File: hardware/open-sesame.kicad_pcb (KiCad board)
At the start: 2 copper layers, 72.2 x 45 mm, 9 parts, among them J1 Conn_01x10, J3 Barrel_Jack_Switch, J4 Conn_01x06_Socket

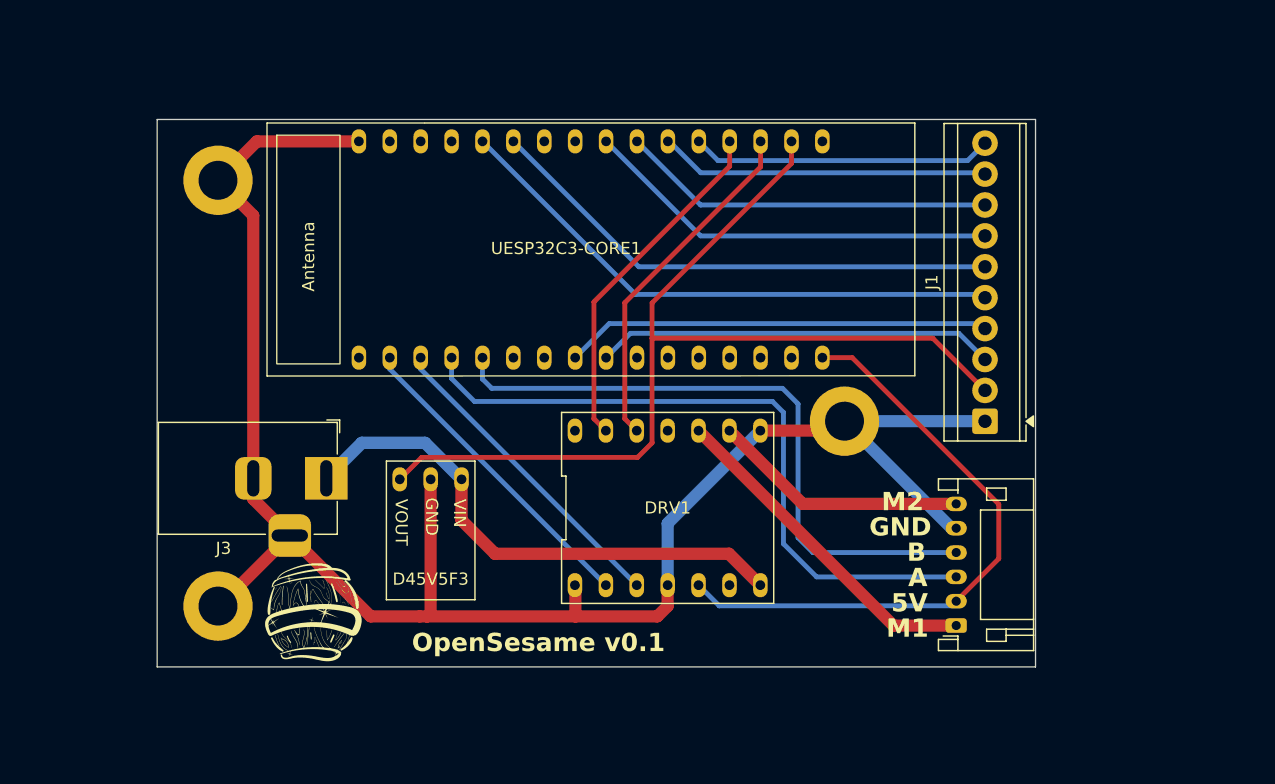
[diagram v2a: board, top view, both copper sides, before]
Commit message: User Terminals, Added Optocoupler, Added QWIIC connector
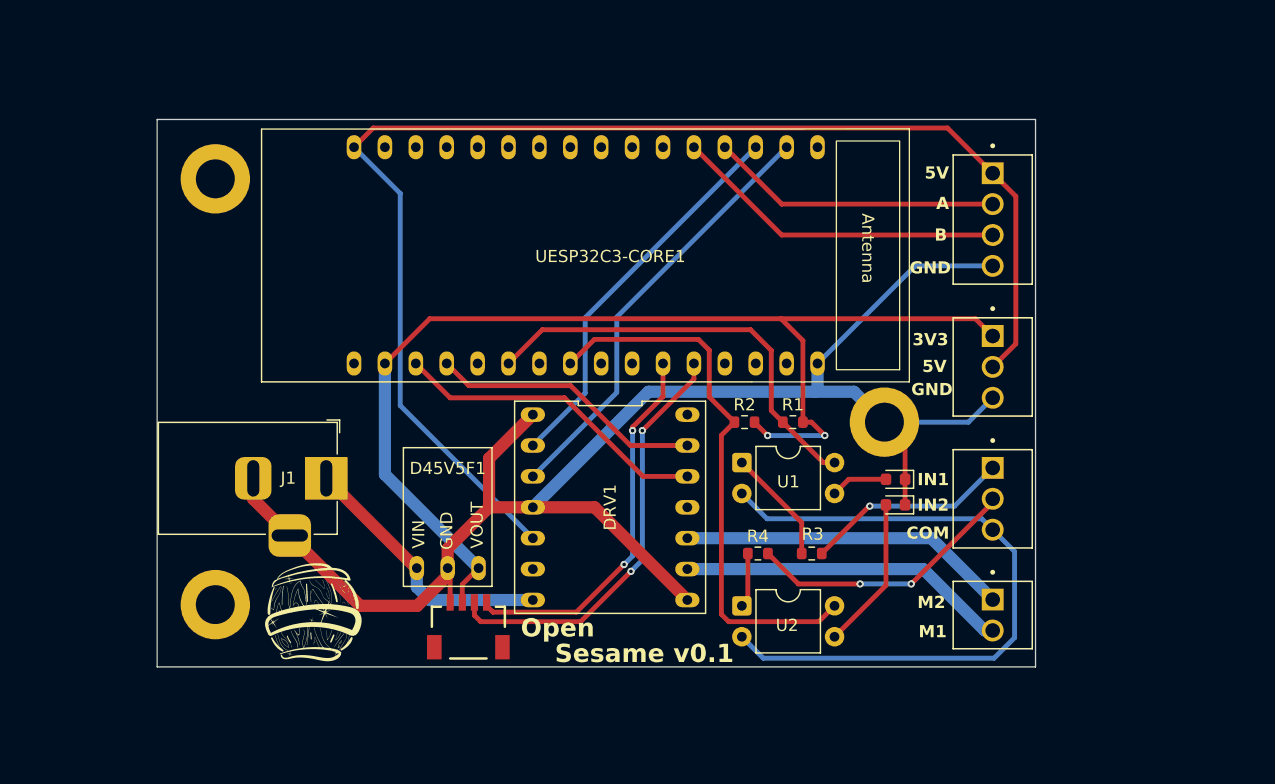
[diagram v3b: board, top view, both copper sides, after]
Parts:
- removed D45V5F3: D45V5F3, Library:D45V5Fx
- removed the J1 at (188.9, 92.4)
- added D1: LED, LED_SMD:LED_0603_1608Metric, F.Cu at (181.5, 97.2)
- added D2: LED, LED_SMD:LED_0603_1608Metric, F.Cu at (181.5, 99.3)
- added D45V5F1: D45V5F3, MyLibrary:D45V5Fx, F.Cu at (144.7, 104.5)
- added J2: Screw_Terminal_01x02, MyLibrary:TE_282834-2, F.Cu at (189.5, 108.4)
- added J3: Screw_Terminal_01x04, MyLibrary:TE_282834-4, F.Cu at (189.5, 75.8)
- added J5: Screw_Terminal_01x03, MyLibrary:TE_282834-3, F.Cu at (189.5, 88.0)
- added J6: Qwiic_RA, SparkFun-Connector:JST_1x04_P1.0mm_Horizontal_SMD, F.Cu at (146.4, 107.3)
- added R1: 10k, Resistor_SMD:R_0603_1608Metric, F.Cu at (173.1, 92.5)
- added R2: 10k, Resistor_SMD:R_0603_1608Metric, F.Cu at (169.1, 92.5)
- added R3: 4.7k, Resistor_SMD:R_0603_1608Metric, F.Cu at (174.6, 103.3)
- added R4: 4.7k, Resistor_SMD:R_0603_1608Metric, F.Cu at (170.2, 103.3)
- added U1: PC817, Package_DIP:DIP-4_W7.62mm, F.Cu at (168.9, 95.8)
- added U2: PC817, Package_DIP:DIP-4_W7.62mm, F.Cu at (168.9, 107.6)
- DRV1: footprint Library:DRV8874 -> MyLibrary:DRV8874
- J4: value Conn_01x06_Socket -> Screw_Terminal_01x03; footprint Connector_JST:JST_PH_S6B-PH-K_1x06_P2.00mm_Horizontal -> MyLibrary:TE_282834-3
- UESP32C3-CORE1: footprint Library:LUATOS_ESP32C3 -> MyLibrary:LUATOS_ESP32C3
- moved J4 10.8 mm to (189.5, 98.8), turned to -90 degrees
- moved DRV1 4.73 mm to (158.1, 99.5), turned to -90 degrees
- moved H2 3.28 mm to (180.6, 92.5)
- moved UESP32C3-CORE1 0.62 mm to (156.1, 78.8), turned to 180 degrees
- moved H1 0.25 mm to (125.6, 72.5)
- moved H3 0.25 mm to (125.6, 107.5), turned to 90 degrees
- renumbered J3 to J1
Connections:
- DRV1 pad 2: Net-(DRV1-EN/IN1) -> EN
- DRV1 pad 3: Net-(DRV1-PH/IN2) -> PH
- J4 pad 1: M2 -> IN1
- J4 pad 2: +5V -> IN2
- J4 pad 3: A -> IN_COMMON
- UESP32C3-CORE1 pad 2: Net-(DRV1-EN/IN1) -> PH
- UESP32C3-CORE1 pad 21: Net-(J1-Pin_10) -> unconnected-(UESP32C3-CORE1-GPIO10/SPI_MISO-Pad21)
- UESP32C3-CORE1 pad 22: Net-(J1-Pin_9) -> GPIO6
- UESP32C3-CORE1 pad 23: Net-(J1-Pin_8) -> unconnected-(UESP32C3-CORE1-GPIO07/SPI_CS-Pad23)
- UESP32C3-CORE1 pad 24: Net-(J1-Pin_7) -> GPIO11
- UESP32C3-CORE1 pad 27: Net-(J1-Pin_6) -> SCL
- UESP32C3-CORE1 pad 28: Net-(J1-Pin_5) -> SDA
- UESP32C3-CORE1 pad 3: Net-(DRV1-PH/IN2) -> EN
- UESP32C3-CORE1 pad 8: Net-(J1-Pin_4) -> unconnected-(UESP32C3-CORE1-UART0_RX-Pad8)
- UESP32C3-CORE1 pad 9: Net-(J1-Pin_3) -> unconnected-(UESP32C3-CORE1-UART0_TX-Pad9)
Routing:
- net +5V: track 50.4 -> 110.4 mm
- net IN_COMMON: track 0.00 -> 55.3 mm
- net Net-(J1-Pin_5): track 46.2 -> 0.00 mm
- net GPIO11: track 0.00 -> 45.7 mm
- net Net-(J1-Pin_6): track 43.0 -> 0.00 mm
- net PH: track 0.00 -> 35.7 mm
- net GPIO6: track 0.00 -> 35.4 mm
- net SDA: track 0.00 -> 35.1 mm, vias 0 -> 2
- net Net-(J1-Pin_4): track 34.4 -> 0.00 mm
- net Net-(J1-Pin_7): track 34.4 -> 0.00 mm
- net Net-(J1-Pin_3): track 32.9 -> 0.00 mm
- net A: track 56.3 -> 24.0 mm
- net EN: track 0.00 -> 32.1 mm
- net SCL: track 0.00 -> 31.3 mm, vias 0 -> 2
- net Net-(J1-Pin_8): track 30.8 -> 0.00 mm
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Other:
- board text added: "3V3"
- board text added: "COM"
- board text added: "IN1"
- board text added: "IN2"
- board text added: "Open"
- board text added: "Sesame v0.1"
- board text removed: "OpenSesame v0.1"

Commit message: Use 2x 6 port connectors
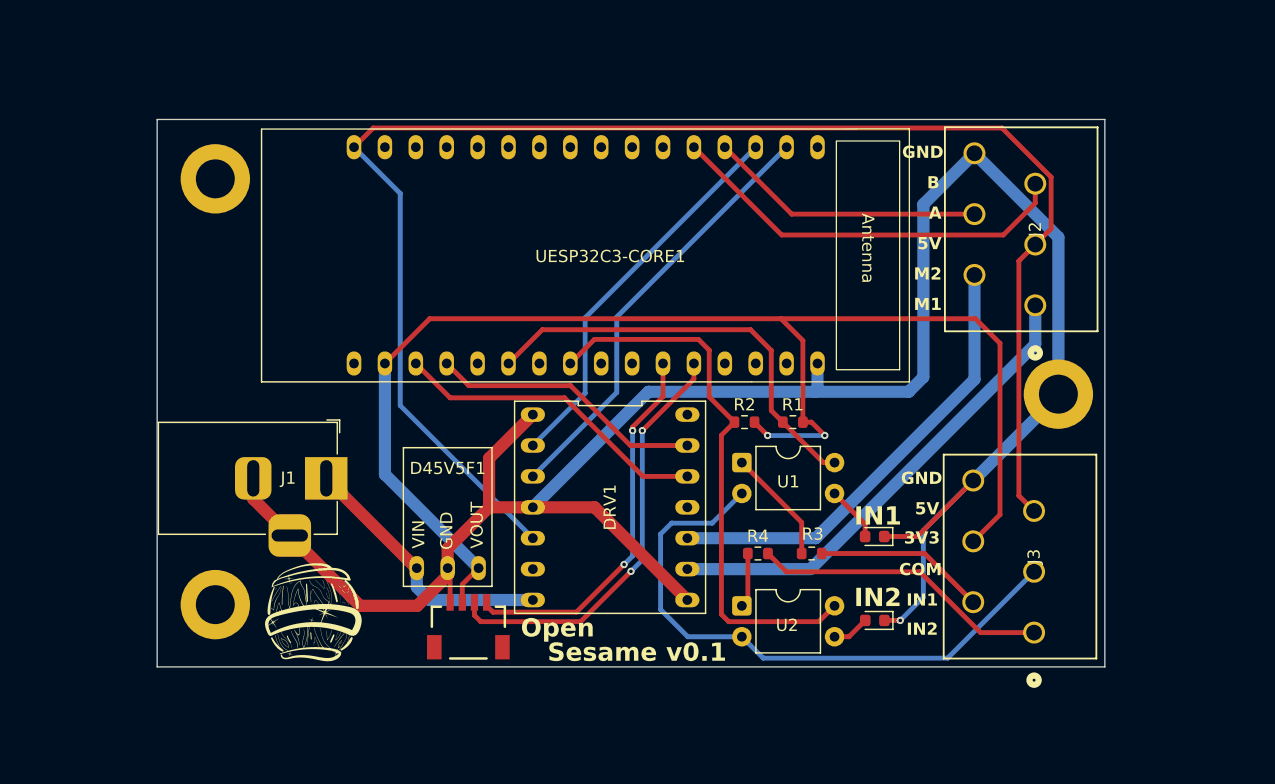
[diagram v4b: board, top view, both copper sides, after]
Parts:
- removed the J4 at (189.5, 98.8)
- removed J5: Screw_Terminal_01x03, MyLibrary:TE_282834-3
- J2: value Screw_Terminal_01x02 -> 1-2834021-6; footprint MyLibrary:TE_282834-2 -> TE-Connectivity-Connector:CONN6_1-2834021-6_TEC
- J3: value Screw_Terminal_01x04 -> 1-2834021-6; footprint MyLibrary:TE_282834-4 -> TE-Connectivity-Connector:CONN6_1-2834021-6_TEC
- moved J3 34.1 mm to (192.9, 109.8), turned to 90 degrees
- moved J2 25.7 mm to (193.0, 82.9), turned to 90 degrees
- moved H2 14.5 mm to (194.9, 90.2)
- moved D2 9.65 mm to (179.8, 108.8)
- moved D1 5.00 mm to (179.8, 101.9)
- renumbered J6 to J4
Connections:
- J2 pad 1: M2 -> M1
- J2 pad 2: M1 -> M2
- J3 pad 1: +5V -> IN2
- J3 pad 2: A -> IN1
- J3 pad 3: B -> IN_COMMON
- J3 pad 4: GND -> +3V3
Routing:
- net GND: track 129.7 -> 177.2 mm, vias 0 -> 1
- net +3V3: track 93.2 -> 111.2 mm
- net +5V: track 110.4 -> 126.9 mm
- net M1: track 27.2 -> 39.5 mm
- net M2: track 27.2 -> 37.6 mm
- net Net-(D2-A): track 12.6 -> 3.08 mm
- net B: track 27.5 -> 33.7 mm
- net IN_COMMON: track 55.3 -> 49.6 mm
- net IN1: track 17.0 -> 14.1 mm, vias 1 -> 0
- net IN2: track 22.3 -> 24.6 mm, vias 2 -> 0
- net A: track 24.0 -> 22.8 mm
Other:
- board size 72.2 x 45 mm -> 77.9 x 45 mm

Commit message: hardware: Use ESP32S3 for PCNT,
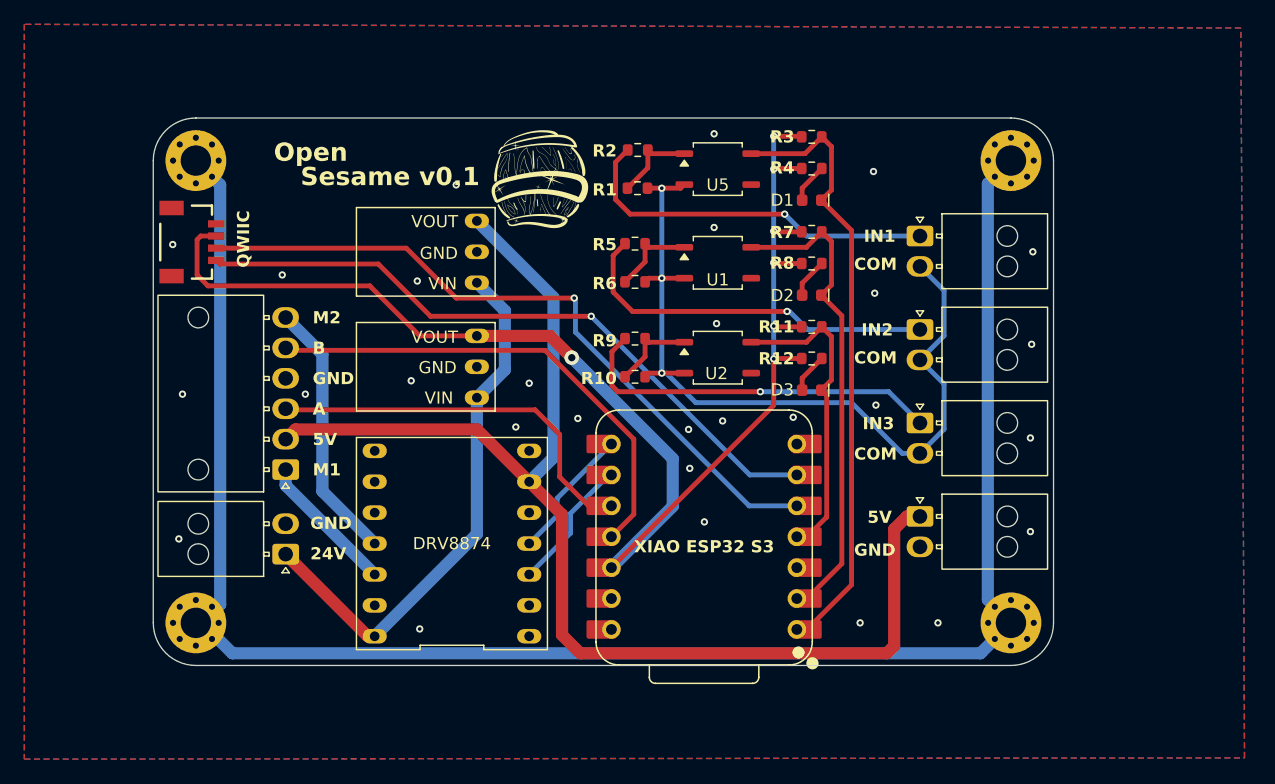
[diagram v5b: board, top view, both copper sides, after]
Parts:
- removed DRV1: DRV8874, MyLibrary:DRV8874
- removed UESP32C3-CORE1: ~, MyLibrary:LUATOS_ESP32C3
- added D3: LED, SparkFun-LED:LED_0603_1608Metric, F.Cu at (174.6, 89.9)
- added D45V5F2: D45V5F3, MyLibrary:D45V5Fx, F.Cu at (147.1, 88.0)
- added DRV8874: DRV8874, MyLibrary:DRV8874, F.Cu at (145.1, 102.5)
- added H4: MountingHole_Pad, MountingHole:MountingHole_2.5mm_Pad_Via, F.Cu at (124.0, 109.0)
- added J5: Conn_01x02, Connector_Molex:Molex_Nano-Fit_105313-xx02_1x02_P2.50mm_Horizontal, F.Cu at (183.5, 84.9)
- added J6: Conn_01x02, Connector_Molex:Molex_Nano-Fit_105313-xx02_1x02_P2.50mm_Horizontal, F.Cu at (183.5, 92.6)
- added J7: Qwiic_RA, SparkFun-Connector:JST_1x04_P1.0mm_Horizontal_SMD, F.Cu at (125.7, 77.7)
- added R10: 750R, Resistor_SMD:R_0603_1608Metric, F.Cu at (160.1, 88.8)
- added R11: 10k, Resistor_SMD:R_0603_1608Metric, F.Cu at (174.6, 84.7)
- added R12: 270R, Resistor_SMD:R_0603_1608Metric, F.Cu at (174.6, 87.3)
- added R5: 750R, Resistor_SMD:R_0603_1608Metric, F.Cu at (160.1, 77.8)
- added R6: 750R, Resistor_SMD:R_0603_1608Metric, F.Cu at (160.1, 81.0)
- added R7: 10k, Resistor_SMD:R_0603_1608Metric, F.Cu at (174.6, 76.9)
- added R8: 270R, Resistor_SMD:R_0603_1608Metric, F.Cu at (174.6, 79.5)
- added R9: 750R, Resistor_SMD:R_0603_1608Metric, F.Cu at (160.1, 85.6)
- added U5: CPC1019N, Package_SO:SOP-4_3.8x4.1mm_P2.54mm, F.Cu at (166.9, 71.7)
- added XIAO ESP32 S3: XIAO-ESP32-S3-DIP, XIAO_Series_Footprints:XIAO-ESP32-S3-DIP, F.Cu at (165.8, 101.9)
- D1, D2: footprint LED_SMD:LED_0603_1608Metric -> SparkFun-LED:LED_0603_1608Metric
- D45V5F1: value D45V5F3 -> D45V5F5
- H1, H2, H3: footprint MountingHole:MountingHole_3.2mm_M3_ISO7380_Pad -> MountingHole:MountingHole_2.5mm_Pad_Via
- J1: value Barrel_Jack_Switch -> Conn_01x02; footprint Connector_BarrelJack:BarrelJack_Horizontal -> Connector_Molex:Molex_Nano-Fit_105313-xx02_1x02_P2.50mm_Horizontal
- J2: value 1-2834021-6 -> Conn_01x06; footprint TE-Connectivity-Connector:CONN6_1-2834021-6_TEC -> Connector_Molex:Molex_Nano-Fit_105313-xx06_1x06_P2.50mm_Horizontal
- J3: value 1-2834021-6 -> Conn_01x02; footprint TE-Connectivity-Connector:CONN6_1-2834021-6_TEC -> Connector_Molex:Molex_Nano-Fit_105313-xx02_1x02_P2.50mm_Horizontal
- J4: value Qwiic_RA -> Conn_01x02; footprint SparkFun-Connector:JST_1x04_P1.0mm_Horizontal_SMD -> Connector_Molex:Molex_Nano-Fit_105313-xx02_1x02_P2.50mm_Horizontal
- R1, R2: value 10k -> 750R
- R3: value 4.7k -> 10k
- R4: value 4.7k -> 270R
- U1, U2: value PC817 -> CPC1019N; footprint Package_DIP:DIP-4_W7.62mm -> Package_SO:SOP-4_3.8x4.1mm_P2.54mm
- moved H1 65.4 mm to (191.0, 71.0)
- moved J2 63.1 mm to (131.4, 96.4), turned to 180 degrees
- moved J4 47.8 mm to (183.5, 77.2)
- moved H3 36.5 mm to (124.0, 71.0), turned to 0 degrees
- moved R3 34.2 mm to (174.6, 69.0)
- moved R4 32.0 mm to (174.6, 71.7)
- moved D1 28.1 mm to (174.6, 74.3)
- moved D2 27.2 mm to (174.6, 82.1)
- moved D45V5F1 26.1 mm to (147.1, 78.5), turned to 90 degrees
- moved R2 24.0 mm to (160.3, 70.1)
- moved R1 23.1 mm to (160.3, 73.3)
- moved U2 20.5 mm to (166.9, 87.2)
- moved H2 19.2 mm to (191.0, 109.0)
- moved U1 16.5 mm to (166.9, 79.4)
- moved J3 13.4 mm to (183.5, 100.2), turned to 0 degrees
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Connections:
- D1 pad 1: GND -> GPIO1
- D2 pad 1: GND -> GPIO2
- D45V5F1 pad 3: +3V3 -> +5V
- H1 pad 1: GND -> Earth
- H2 pad 1: GND -> Earth
- H3 pad 1: GND -> Earth
- J2 pad 2: M2 -> +5V
- J2 pad 3: +5V -> A
- J2 pad 4: A -> GND
- J2 pad 6: GND -> M2
- J3 pad 1: IN2 -> +5V
- J3 pad 2: IN1 -> GND
- J4 pad 1: GND -> IN1
- J4 pad 2: +3V3 -> IN_COMMON
- R1 pad 1: GPIO6 -> Net-(R1-Pad1)
- R1 pad 2: +3V3 -> IN_COMMON
- R2 pad 1: GPIO11 -> IN1
- R2 pad 2: +3V3 -> Net-(R1-Pad1)
- R3 pad 1: Net-(R3-Pad1) -> +3V3
- R3 pad 2: IN1 -> GPIO1
- R4 pad 1: Net-(R4-Pad1) -> +3V3
- R4 pad 2: IN2 -> Net-(D1-A)
- U1 pad 1: Net-(R3-Pad1) -> Net-(R5-Pad2)
- U1 pad 3: Net-(D1-A) -> GND
- U1 pad 4: GPIO6 -> GPIO2
- U2 pad 1: Net-(R4-Pad1) -> Net-(R10-Pad1)
- U2 pad 3: Net-(D2-A) -> GND
- U2 pad 4: GPIO11 -> GPIO4
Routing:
- net GND: track 177.2 -> 0.00 mm, vias 1 -> 29
- net Earth: track 0.00 -> 147.6 mm
- net GPIO1: track 0.00 -> 51.2 mm
- net GPIO11: track 45.7 -> 0.00 mm
- net GPIO2: track 0.00 -> 39.0 mm
- net GPIO6: track 35.4 -> 0.00 mm
- net IN3: track 0.00 -> 30.9 mm, vias 0 -> 1
- net M1: track 39.5 -> 11.7 mm
- net FAULT: track 26.2 -> 0.00 mm
- net +5V: track 126.9 -> 101.1 mm
- net GPIO4: track 0.00 -> 25.1 mm
- net PH: track 35.7 -> 11.0 mm
- net SCL: track 31.3 -> 55.0 mm, vias 2 -> 1
- net SDA: track 35.1 -> 58.1 mm, vias 2 -> 1
- net CS: track 22.6 -> 0.00 mm
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- added copper zone on B.Cu, net GND
- added copper zone on F.Cu, net GND
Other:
- board size 77.9 x 45 mm -> 74 x 45 mm
- board text added: "24V"
- board text added: "IN3"
- board text added: "QWIIC"
- board text removed: "3V3"

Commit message: hardware: shrunk board
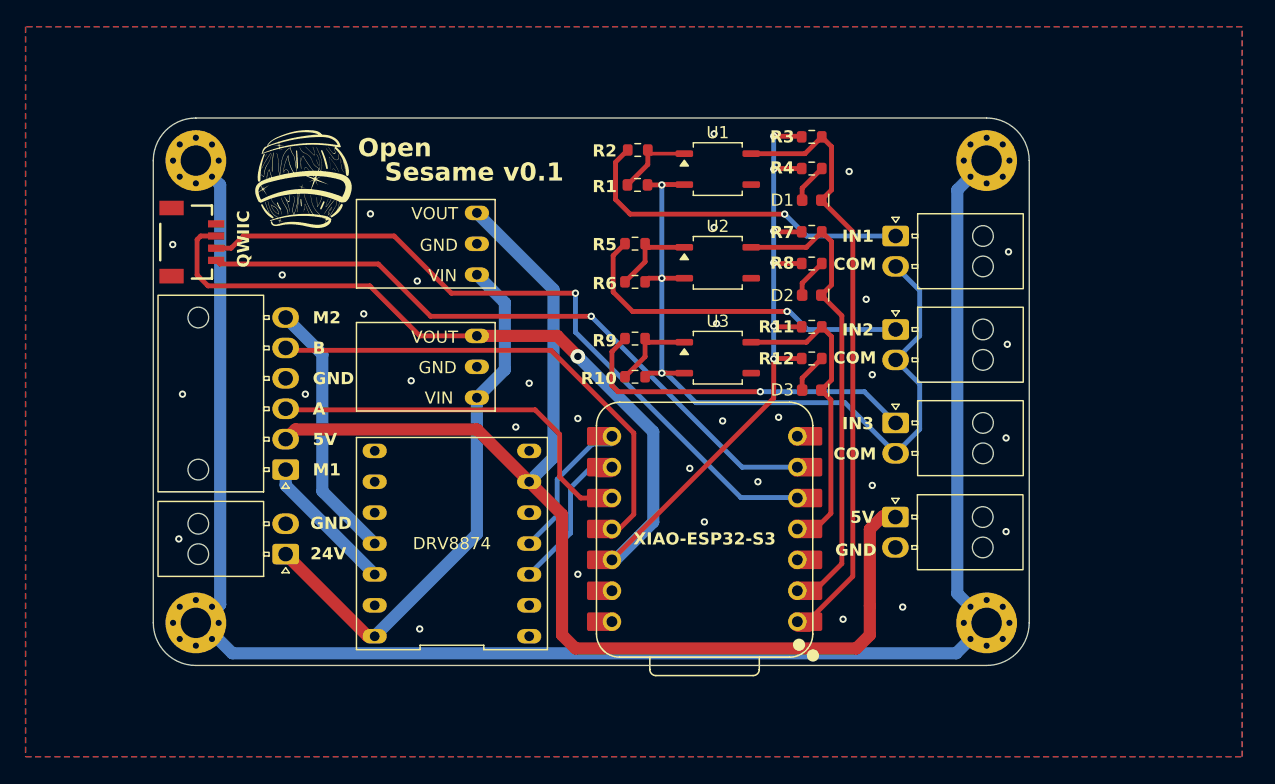
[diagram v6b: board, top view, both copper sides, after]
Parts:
- removed U5: CPC1019N, Package_SO:SOP-4_3.8x4.1mm_P2.54mm
- added U3: CPC1019N, Package_SO:SOP-4_3.8x4.1mm_P2.54mm, F.Cu at (166.9, 87.2)
- XIAO-ESP32-S3: renamed from XIAO ESP32 S3
- moved U2 7.80 mm to (166.9, 79.4)
- moved U1 7.70 mm to (166.9, 71.7)
- moved J3 2.02 mm to (181.5, 100.3)
- moved H1 2.00 mm to (189.0, 71.0)
- moved H2 2.00 mm to (189.0, 109.0)
- moved J4 2.00 mm to (181.5, 77.2)
- moved J5 2.00 mm to (181.5, 84.9)
- moved J6 2.00 mm to (181.5, 92.6)
- moved D45V5F1 0.66 mm to (147.1, 77.8)
- moved XIAO-ESP32-S3 0.64 mm to (165.8, 101.3)
- moved R1 0.27 mm to (160.3, 73.0)
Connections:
- U1 pad 1: Net-(R5-Pad2) -> Net-(R1-Pad1)
- U1 pad 4: GPIO2 -> GPIO1
- U2 pad 1: Net-(R10-Pad1) -> Net-(R5-Pad2)
- U2 pad 4: GPIO4 -> GPIO2
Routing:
- net +5V: track 101.1 -> 98.9 mm
- net +3V3: track 115.9 -> 113.9 mm
- net IN3: track 30.9 -> 28.9 mm
- net IN2: track 30.9 -> 28.9 mm
- net IN1: track 30.7 -> 28.7 mm
- net IN_COMMON: track 67.6 -> 65.8 mm
- net Earth: track 147.6 -> 146.0 mm
- net EN: track 12.2 -> 13.7 mm
- net PH: track 11.0 -> 11.9 mm
- net A: track 31.3 -> 30.4 mm
- net SDA: track 58.1 -> 59.0 mm
- net +24V: track 44.6 -> 45.2 mm
- net GPIO1: track 51.2 -> 50.6 mm
- net GND: vias 29 -> 32
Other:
- board size 74 x 45 mm -> 72 x 45 mm
